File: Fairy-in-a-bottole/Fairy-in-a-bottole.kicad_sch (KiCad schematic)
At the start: 6 parts, among them J1 FTDI, U1 ESP32-WROOM-32D, U2 AMS1117-3.3

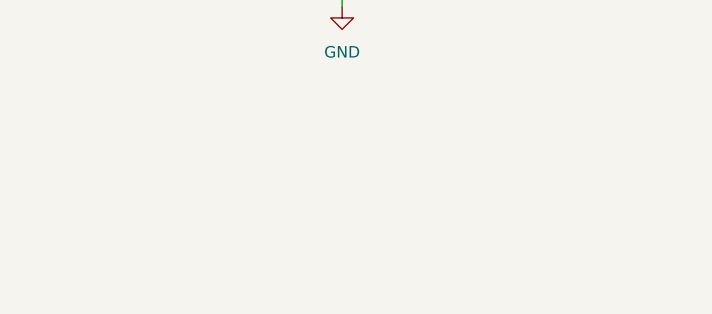
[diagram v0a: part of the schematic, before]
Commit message: added link to usefull battery proection cirucit
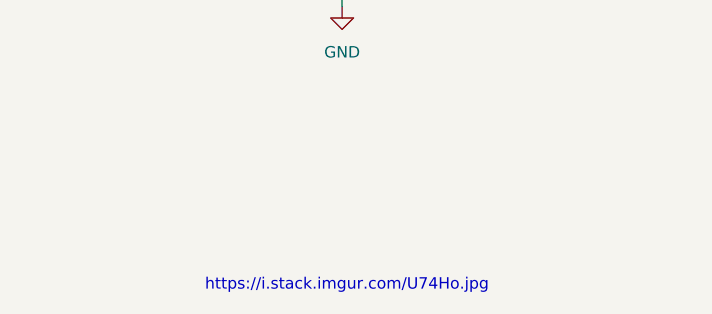
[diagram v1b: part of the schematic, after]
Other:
- note added: "https://i.stack.imgur.com/U74Ho.jpg"
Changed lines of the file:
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@@
     (stroke (width 0) (type default) (color 0 0 0 0))
+  )
+  (text "https://i.stack.imgur.com/U74Ho.jpg" (at 128.27 143.51 0)
+    (effects (font (size 1.27 1.27)) (justify left bottom))
   )
   (label "Reset" (at 146.05 97.79 0)

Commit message: added some parts to it dude
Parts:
- added U?: FS8205A, symbol LIPO:FS8205A
- added U?: DW01A, symbol LIPO:DW01A
- added U?: SLM2169, symbol LIPO:SLM2169
- added U?: BL8573CB6TR, symbol LIPO:BL8573CB6TR
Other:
- note added: "BMS"
- note added: "Boost ic"
- note added: "LiPo charger IC"
- note added: "Wheres my F***ing Sonic?"
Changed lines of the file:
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@@
     (stroke (width 0) (type default) (color 0 0 0 0))
+  )
+  (text "Wheres my F***ing Sonic? " (at 168.91 111.76 0)
+    (effects (font (size 1.27 1.27)) (justify left bottom))
+  )
+  (text "LiPo charger IC\n" (at 24.13 157.48 0)
+    (effects (font (size 1.27 1.27)) (justify left bottom))
+  )
+  (text "Boost ic\n" (at 154.94 156.21 0)
+    (effects (font (size 1.27 1.27)) (justify left bottom))
+  )
+  (text "BMS\n" (at 88.9 146.05 0)
+    (effects (font (size 1.27 1.27)) (justify left bottom))
   )
   (text "https://i.stack.imgur.com/U74Ho.jpg" (at 128.27 143.51 0)
@@
     (pin "2")
     (pin "3")
+  )
+  (symbol (lib_id "LIPO:FS8205A") (at 88.9 182.88 0) (unit 1)
+    (in_bom yes) (on_board yes) (fields_autoplaced)
+    (property "Reference" "U?" (id 0) (at 88.519 166.37 0))
+    (property "Value" "FS8205A" (id 1) (at 88.519 168.91 0))
+    (property "Footprint" "" (id 2) (at 88.9 182.88 0)
+      (effects (font (size 1.27 1.27)) hide)
+    )
+    (property "Datasheet" "" (id 3) (at 88.9 182.88 0)
+      (effects (font (size 1.27 1.27)) hide)
+    )
+    (pin "1")
+    (pin "2")
+    (pin "3")
+    (pin "4")
+    (pin "5")
+    (pin "6")
   )
   (symbol (lib_id "RF_Module:ESP32-WROOM-32D") (at 68.58 83.82 0) (unit 1)
@@
     (pin "1")
   )
+  (symbol (lib_id "LIPO:DW01A") (at 92.71 160.02 0) (unit 1)
+    (in_bom yes) (on_board yes) (fields_autoplaced)
+    (property "Reference" "U?" (id 0) (at 92.075 151.13 0))
+    (property "Value" "DW01A" (id 1) (at 92.075 153.67 0))
+    (property "Footprint" "" (id 2) (at 92.71 160.02 0)
+      (effects (font (size 1.27 1.27)) hide)
+    )
+    (property "Datasheet" "" (id 3) (at 92.71 160.02 0)
+      (effects (font (size 1.27 1.27)) hide)
+    )
+    (pin "1")
+    (pin "2")
+    (pin "3")
+    (pin "4")
+    (pin "5")
+    (pin "6")
+  )
+  (symbol (lib_id "LIPO:SLM2169") (at 158.75 171.45 0) (unit 1)
+    (in_bom yes) (on_board yes) (fields_autoplaced)
+    (property "Reference" "U?" (id 0) (at 160.7694 160.02 0)
+      (effects (font (size 1.27 1.27)) (justify left))
+    )
+    (property "Value" "SLM2169" (id 1) (at 160.7694 162.56 0)
+      (effects (font (size 1.27 1.27)) (justify left))
+    )
+    (property "Footprint" "" (id 2) (at 158.75 171.45 0)
+      (effects (font (size 1.27 1.27)) hide)
+    )
+    (property "Datasheet" "" (id 3) (at 158.75 171.45 0)
+      (effects (font (size 1.27 1.27)) hide)
+    )
+    (pin "1")
+    (pin "2")
+    (pin "3")
+    (pin "4")
+    (pin "5")
+  )
+  (symbol (lib_id "LIPO:BL8573CB6TR") (at 29.21 172.72 0) (unit 1)
+    (in_bom yes) (on_board yes) (fields_autoplaced)
+    (property "Reference" "U?" (id 0) (at 31.2294 161.29 0)
+      (effects (font (size 1.27 1.27)) (justify left))
+    )
+    (property "Value" "BL8573CB6TR" (id 1) (at 31.2294 163.83 0)
+      (effects (font (size 1.27 1.27)) (justify left))
+    )
+    (property "Footprint" "" (id 2) (at 29.21 151.13 0)
+      (effects (font (size 1.27 1.27)) hide)
+    )
+    (property "Datasheet" "" (id 3) (at 29.21 151.13 0)
+      (effects (font (size 1.27 1.27)) hide)
+    )
+    (pin "")
+    (pin "1")
+    (pin "2")
+    (pin "4")
+    (pin "5")
+    (pin "6")
+  )
   (symbol (lib_id "power:GND") (at 68.58 121.92 0) (unit 1)
     (in_bom yes) (on_board yes) (fields_autoplaced)
@@
       (reference "U2") (unit 1) (value "AMS1117-3.3") (footprint "Package_TO_SOT_SMD:SOT-223-3_TabPin2")
     )
-  )
+    (path "/23751b29-0ec6-4a47-bc1a-2ae88f43245d"
+      (reference "U?") (unit 1) (value "FS8205A") (footprint "")
+    )
+    (path "/59850d98-9bd9-49b7-a34a-5737e392d80a"
+      (reference "U?") (unit 1) (value "DW01A") (footprint "")
+    )
+    (path "/692bbab5-215e-42d2-9a48-a0dac0b31885"
+      (reference "U?") (unit 1) (value "SLM2169") (footprint "")
+    )
+    (path "/7ccb64a4-5140-45d8-b9b5-dda5ed655627"
+      (reference "U?") (unit 1) (value "BL8573CB6TR") (footprint "")
+    )
+  )

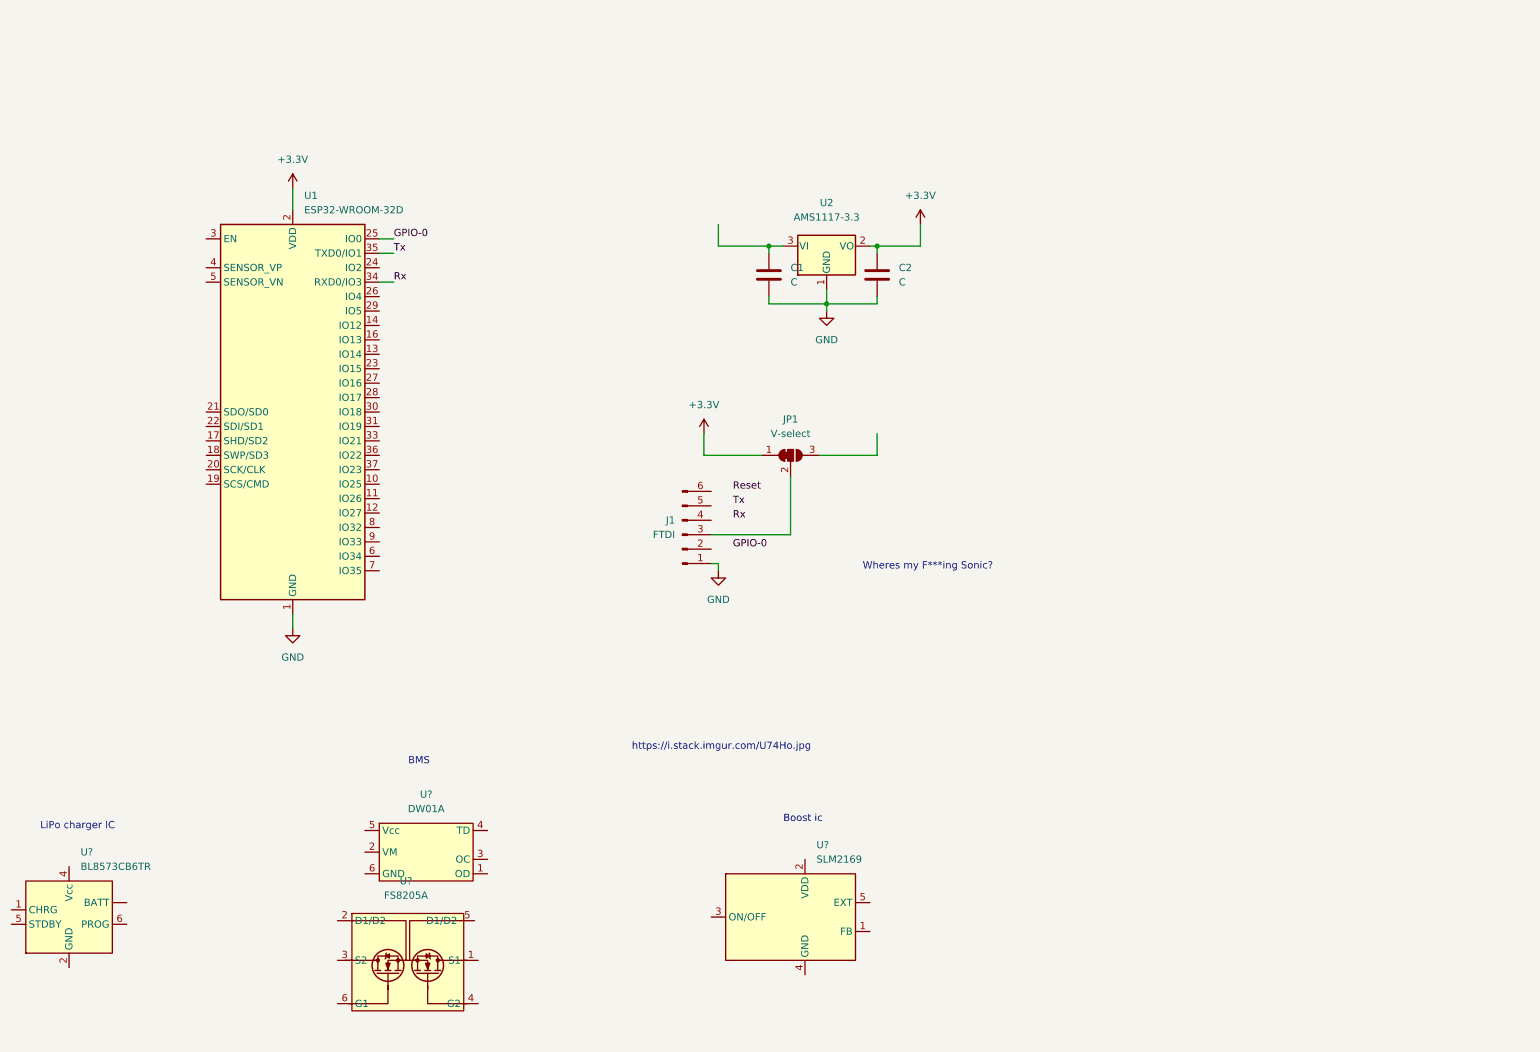
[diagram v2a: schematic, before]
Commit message: updated scimatic symbols as they were on the wrong grid size :/ and wired in a lose ciruit for how it should work, still gotta check stuff.
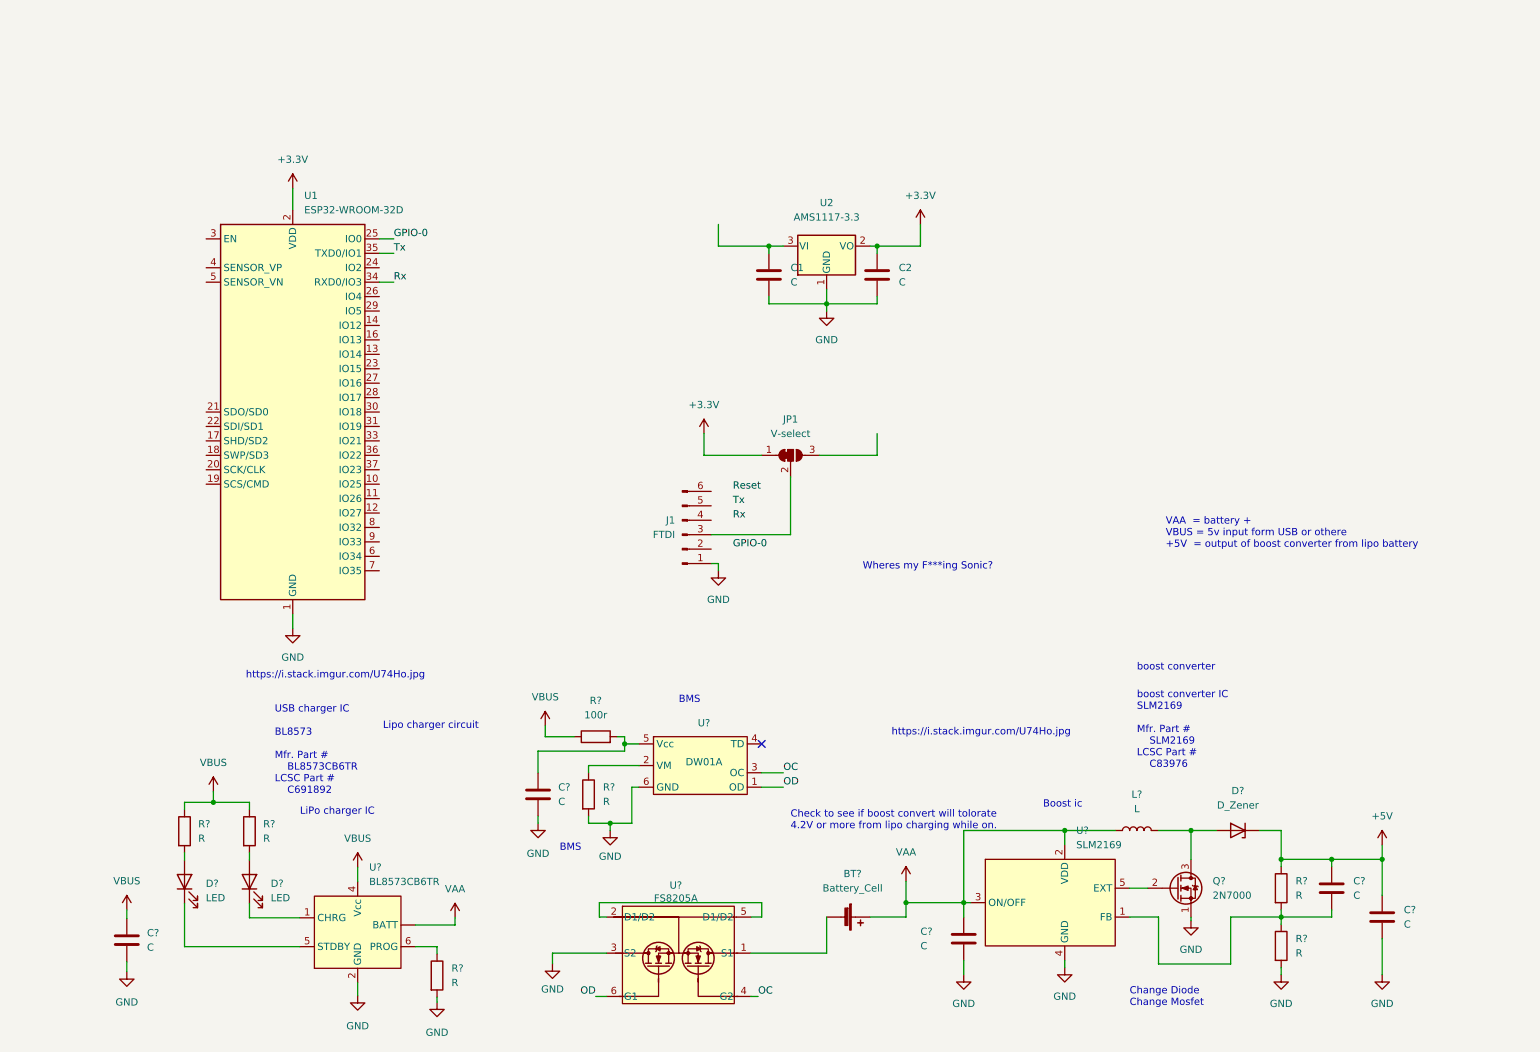
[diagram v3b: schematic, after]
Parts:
- removed U?: FS8205A, symbol LIPO:FS8205A
- removed U?: DW01A, symbol LIPO:DW01A
- removed U?: SLM2169, symbol LIPO:SLM2169
- removed U?: BL8573CB6TR, symbol LIPO:BL8573CB6TR
- added BT?: Battery_Cell, Battery:BatteryHolder_Keystone_1042_1x18650, symbol Device:Battery_Cell
- added C? (x5): C, Capacitor_SMD:C_0805_2012Metric_Pad1.18x1.45mm_HandSolder, symbol Device:C
- added D? (x2): LED, Diode_SMD:D_3220_8050Metric_Pad2.65x5.15mm_HandSolder, symbol Device:LED
- added D?: D_Zener, symbol Device:D_Zener
- added L?: L, symbol Device:L
- added Q?: 2N7000, Package_TO_SOT_THT:TO-92_Inline, symbol Transistor_FET:2N7000
- added R? (x6): R, Resistor_SMD:R_0603_1608Metric, symbol Device:R
- added R?: 100r, Resistor_SMD:R_0603_1608Metric, symbol Device:R
- added U?: BL8573CB6TR, symbol lipo stuff:BL8573CB6TR
- added U?: DW01A, symbol lipo stuff:DW01A
- added U?: FS8205A, symbol lipo stuff:FS8205A
- added U?: SLM2169, symbol lipo stuff:SLM2169
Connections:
- net GND: now also C?.2, C?.2, C?.2, C?.2, Q?.1 (S), R?.2, R?.2, R?.2, U?.2 (GND), U?.3 (S2), U?.4 (GND), U?.6 (GND)
- new net: D?.1 (K), U?.5 (STDBY)
- new net: D?.2 (A), R?.2 (x2)
- new net: D?.1 (K), U?.1 (CHRG)
- new net: R?.1, U?.6 (PROG)
- new net: C?.2, R?.1, R?.2, U?.1 (FB)
- new net: R?.1, U?.2 (VM)
- new net: C?.1, R?.2, U?.5 (Vcc)
- new net: D?.2 (A), L?.2, Q?.3 (D)
- new net: Q?.2 (G), U?.5 (EXT)
- new net: BT?.2 (-), U?.1 (S1)
- new net: U?.2 (D1/D2), U?.5 (D1/D2)
- new net +5V: C?.1, C?.1, D?.1 (K), R?.1
- new net OC: U?.3 (OC), U?.4 (G2)
- new net OD: U?.1 (OD), U?.6 (G1)
- new net VAA: BT?.1 (+), C?.1, L?.1, U?. (BATT), U?.2 (VDD), U?.3 (ON/OFF)
- new net VBUS: C?.1, R?.1, R?.1, R?.1, U?.4 (Vcc)
- no-connect marks 0 -> 1
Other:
- note added: "Change Diode Change Mosfet"
- note added: "Check to see if boost convert will tolorate 4.2V or more from lipo charging while on."
- note added: "Lipo charger circuit"
- note added: "USB charger IC BL8573 Mfr. Part # BL8573CB6TR LCSC Part # C691892"
- note added: "VAA = battery + VBUS = 5v input form USB or othere +5V = output of boost converter from lipo battery"
- note added: "boost converter"
- note added: "boost converter IC SLM2169 Mfr. Part # SLM2169 LCSC Part # C83976"

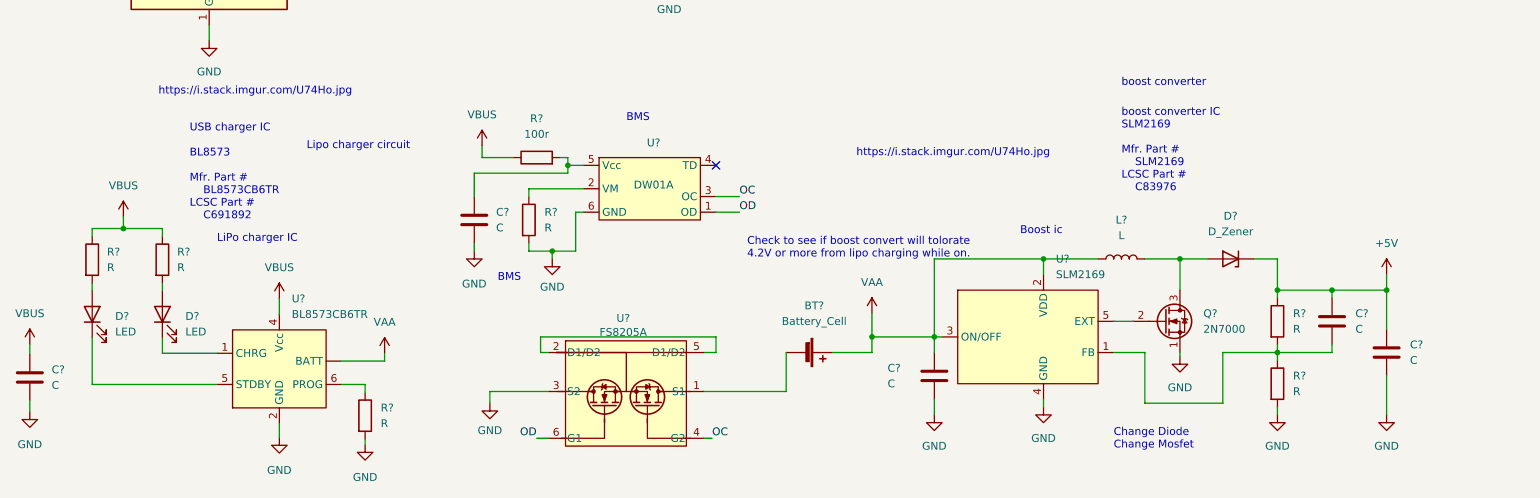
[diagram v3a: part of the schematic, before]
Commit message: added footprints for the most components
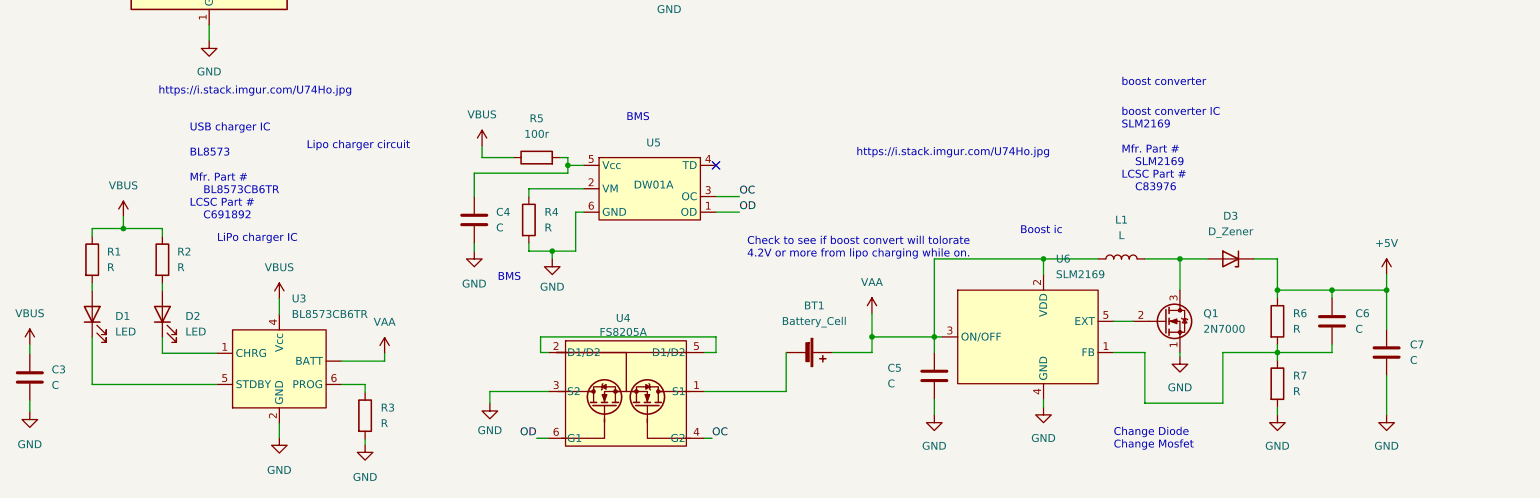
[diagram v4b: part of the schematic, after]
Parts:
- U3, U4, U5: renamed from U?; footprint (none) -> Package_TO_SOT_SMD:SOT-23-6
- U6: renamed from U?; footprint (none) -> Package_TO_SOT_SMD:SOT-23-5
- gave numbers to parts that had none: 18
